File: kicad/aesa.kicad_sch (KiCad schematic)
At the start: 0 parts

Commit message: AD7606C-16, one sheet per repeated block, clock buffering, first simulations
- ADC: AD7606C-16 in software mode (OS pins high, WR held high, DB11/SDI on
  shared ADC_SDI), 33 R source resistors on DOUTA/DOUTB/BUSY.
- Every repeated block is its own reused sheet: tx_group x16, en_buf x4,
  clk_buf x7, mic x8 (replaces tx_shift, tx_drivers, mems). Sheets other than
  channel are generated by scripts/build_cells.py and scripts/build_power.py.
- Headers: GND conductors either side of every clock, ADC_SDI, idle pulls,
  DNP RC terminations as fallback.
- Power: 3V3_MIC ferrite filter moved to the power sheet with LED, test point
  and flag.
- Simulations (LTspice, sim/): RX chain gain/noise, TX burst and recovery,
  clock signal integrity; results in docs/simulation-1.md. FPGA ribbon outputs
  changed to DRIVE 4 after simulation.
- Brief, CLAUDE.md, review status and SKiDL reference spec updated.
  ERC: 0 violations, 1,701 parts.
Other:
- removed sheet MEMS mics
- removed sheet TX gate drivers
- removed sheet TX shift registers
- added sheet CLKB1 (clk_buf.kicad_sch)
- added sheet CLKB2 (clk_buf.kicad_sch)
- added sheet CLKB3 (clk_buf.kicad_sch)
- added sheet CLKB4 (clk_buf.kicad_sch)
- added sheet CLKB5 (clk_buf.kicad_sch)
- added sheet CLKB6 (clk_buf.kicad_sch)
- added sheet CLKB7 (clk_buf.kicad_sch)
- added sheet MIC1 (mic.kicad_sch)
- added sheet MIC2 (mic.kicad_sch)
- added sheet MIC3 (mic.kicad_sch)
- added sheet MIC4 (mic.kicad_sch)
- added sheet MIC5 (mic.kicad_sch)
- added sheet MIC6 (mic.kicad_sch)
- added sheet MIC7 (mic.kicad_sch)
- added sheet MIC8 (mic.kicad_sch)
- added sheet TXEN1 (en_buf.kicad_sch)
- added sheet TXEN2 (en_buf.kicad_sch)
- added sheet TXEN3 (en_buf.kicad_sch)
- added sheet TXEN4 (en_buf.kicad_sch)
- added sheet TXG01 (tx_group.kicad_sch)
- added sheet TXG02 (tx_group.kicad_sch)
- added sheet TXG03 (tx_group.kicad_sch)
- added sheet TXG04 (tx_group.kicad_sch)
- added sheet TXG05 (tx_group.kicad_sch)
- added sheet TXG06 (tx_group.kicad_sch)
- added sheet TXG07 (tx_group.kicad_sch)
- added sheet TXG08 (tx_group.kicad_sch)
- added sheet TXG09 (tx_group.kicad_sch)
- added sheet TXG10 (tx_group.kicad_sch)
- added sheet TXG11 (tx_group.kicad_sch)
- added sheet TXG12 (tx_group.kicad_sch)
- added sheet TXG13 (tx_group.kicad_sch)
- added sheet TXG14 (tx_group.kicad_sch)
- added sheet TXG15 (tx_group.kicad_sch)
- added sheet TXG16 (tx_group.kicad_sch)
- sheet ADC1 ports: added CONVST, SCLK; removed none
- sheet ADC2 ports: added CONVST, SCLK; removed none
- sheet ADC3 ports: added CONVST, SCLK; removed none
- sheet ADC4 ports: added CONVST, SCLK; removed none
- sheet ADC5 ports: added CONVST, SCLK; removed none
- sheet ADC6 ports: added CONVST, SCLK; removed none
- sheet ADC7 ports: added CONVST, SCLK; removed none
- sheet ADC8 ports: added CONVST, SCLK; removed none

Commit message: Block-diagram top page, power review fixes, readable sheets
Top level
- Page 1 is now a block diagram of the signal flow (FPGA -> headers ->
  clock buffers / TX drive -> transceivers -> ADCs -> FPGA, mics, power).
- New group sheets hold the reused cells: tx (16 tx_group + 4 en_buf),
  array (64 channel), adcs (8 adc), mics (8 mic), clocks (7 clk_buf).
  Power and headers stay directly under the top. All written by gen_top.py,
  which now also survives a kicad-cli re-save of a cell sheet.

Power (review findings)
- Polyfuse 1812L200/16DR (16 V), TPS65131RGER stated explicitly, input caps
  2 x 10u 1206, 50 V caps on 12 V, inductor values carry minimum Isat.
- +3V3: TLV75733P (ceramic-stable) replaces TLV1117-33.
- New JP5/JP6 isolate +-6V5; every rail: REG node -> jumper -> rail with TP,
  LED (not on analog LDOs) and PWR_FLAG.
- Power sheet is now generated by build_cells.py in a 2x3 block layout
  (build_power.py removed).

Readability and small fixes
- Rails on sideways pins use labelled flags; sideways GND symbols hide text.
- tx_group: 595 outputs wired straight to the drivers.
- Title blocks on every sheet; channel sheet notes and field placement fixed
  (sch_fields.py --only, sch_annotate.py).
- ADC_SDI 10k pull-down, ADC reset/DOUT notes, mic cap 50 V.
- ERC 0 violations, 1,704 parts. PDFs: docs/schematics/00..13.
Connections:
- no-connect marks 7 -> 0
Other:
- removed sheet ADC1
- removed sheet ADC2
- removed sheet ADC3
- removed sheet ADC4
- removed sheet ADC5
- removed sheet ADC6
- removed sheet ADC7
- removed sheet ADC8
- removed sheet AXU3EGB headers
- removed sheet CH01
- removed sheet CH02
- removed sheet CH03
- removed sheet CH04
- removed sheet CH05
- removed sheet CH06
- removed sheet CH07
- removed sheet CH08
- removed sheet CH09
- removed sheet CH10
- removed sheet CH11
- removed sheet CH12
- removed sheet CH13
- removed sheet CH14
- removed sheet CH15
- removed sheet CH16
- removed sheet CH17
- removed sheet CH18
- removed sheet CH19
- removed sheet CH20
- removed sheet CH21
- removed sheet CH22
- removed sheet CH23
- removed sheet CH24
- removed sheet CH25
- removed sheet CH26
- removed sheet CH27
- removed sheet CH28
- removed sheet CH29
- removed sheet CH30
- removed sheet CH31
- removed sheet CH32
- removed sheet CH33
- removed sheet CH34
- removed sheet CH35
- removed sheet CH36
- removed sheet CH37
- removed sheet CH38
- removed sheet CH39
- removed sheet CH40
- removed sheet CH41
- removed sheet CH42
- removed sheet CH43
- removed sheet CH44
- removed sheet CH45
- removed sheet CH46
- removed sheet CH47
- removed sheet CH48
- removed sheet CH49
- removed sheet CH50
- removed sheet CH51
- removed sheet CH52
- removed sheet CH53
- removed sheet CH54
- removed sheet CH55
- removed sheet CH56
- removed sheet CH57
- removed sheet CH58
- removed sheet CH59
- removed sheet CH60
- removed sheet CH61
- removed sheet CH62
- removed sheet CH63
- removed sheet CH64
- removed sheet CLKB1
- removed sheet CLKB2
- removed sheet CLKB3
- removed sheet CLKB4
- removed sheet CLKB5
- removed sheet CLKB6
- removed sheet CLKB7
- removed sheet MIC1
- removed sheet MIC2
- removed sheet MIC3
- removed sheet MIC4
- removed sheet MIC5
- removed sheet MIC6
- removed sheet MIC7
- removed sheet MIC8
- removed sheet TXEN1
- removed sheet TXEN2
- removed sheet TXEN3
- removed sheet TXEN4
- removed sheet TXG01
- removed sheet TXG02
- removed sheet TXG03
- removed sheet TXG04
- removed sheet TXG05
- removed sheet TXG06
- removed sheet TXG07
- removed sheet TXG08
- removed sheet TXG09
- removed sheet TXG10
- removed sheet TXG11
- removed sheet TXG12
- removed sheet TXG13
- removed sheet TXG14
- removed sheet TXG15
- removed sheet TXG16
- added sheet ADCs (adcs.kicad_sch)
- added sheet Clock buffers (clocks.kicad_sch)
- added sheet FPGA headers J1/J2 (headers.kicad_sch)
- added sheet MEMS mics (mics.kicad_sch)
- added sheet TX drive (tx.kicad_sch)
- added sheet Transceivers (array.kicad_sch)
- note added: "(ADCs)"
- note added: "(TX, mics)"
- note added: "(off-board)"
- note added: "0 / 15 V"
- note added: "1. The FPGA streams one TX bit per element (16 serial lines, 10 MHz) and the clocks."
- note added: "12 V jack -> +5V, +-6V5, +-5VA (analog), VDRV 15 V (TX), +3V3, 3V3_MIC."
- note added: "16 x 74HCT595 + 32 x UCC27524"
- note added: "2 ribbons"
- note added: "2. TX drive: shift registers latch the bits; gate drivers switch each element between 0 and 15 V."
- note added: "3. Transceivers: the 64 CUSA-TR65 elements emit 40 kHz; echoes return to the same elements."
- note added: "4 x enable buffer"
- note added: "4. The diode T/R switch and limiter protect the receiver; amplifier + 40 kHz band-pass give x22."
- note added: "40 kHz"
- note added: "5. ADCs: 8 x AD7606C-16 sample all 64 channels at 200 kSPS (raw waveform, amplitude and phase)."
- note added: "6. The samples go back to the FPGA over the ribbon, which forms the beams. 8 MEMS mics add wideband audio."
- note added: "64 x: T/R diodes, CUSA-TR65,"
- note added: "7 x 74LVC2G34, 33 R"
- note added: "8 x AD7606C-16, 200 kSPS"
- note added: "8 x SPH0641 PDM"
- note added: "ADC readout"
- note added: "ADC_DOUTA/B 1-8, BUSY"
- note added: "ALINX AXU3EGB"
- note added: "Air /"
- note added: "Click a block to open it. Repeated parts are one sheet each: channel x64, adc x8, tx_group x16, en_buf x4, clk_buf x7, mic x8."
- note added: "DRV1-64"
- note added: "Every rail: test point, isolation jumper, LED (not on the analog LDOs)."
- note added: "Hybrid 8x8 ultrasonic AESA: how the signal flows"
- note added: "J1 = AXU3EGB J15"
- note added: "J2 = AXU3EGB J16"
- note added: "MIC_DATA0-3 (PDM)"
- note added: "PDM clock"
- note added: "RX1-64"
- note added: "SCK, LATCH"
- note added: "SCLK, CONVST"
- note added: "TX timing,"
- note added: "TX_SDI0-15, TX_EN, /OE, /CLR"
- note added: "Zynq UltraScale+"
- note added: "beamforming,"
- note added: "clocks"
- note added: "echo"
- note added: "echo x22"
- note added: "limiter, x6 amp, 40 kHz band-pass"
- note added: "target"
- note removed: "Hybrid 8x8 ultrasonic AESA: 64 transceiver channels (CH01..CH64, one sheet reused 64 times), 8 MEMS mics, 8 ADCs. Source of truth: this KiCad hierarchy; skidl/channel.py is the reference spec."
- company: (none) -> Hybrid 8x8 ultrasonic AESA
- title: Ultrasonic AESA front end -> Hybrid 8x8 ultrasonic AESA: block diagram

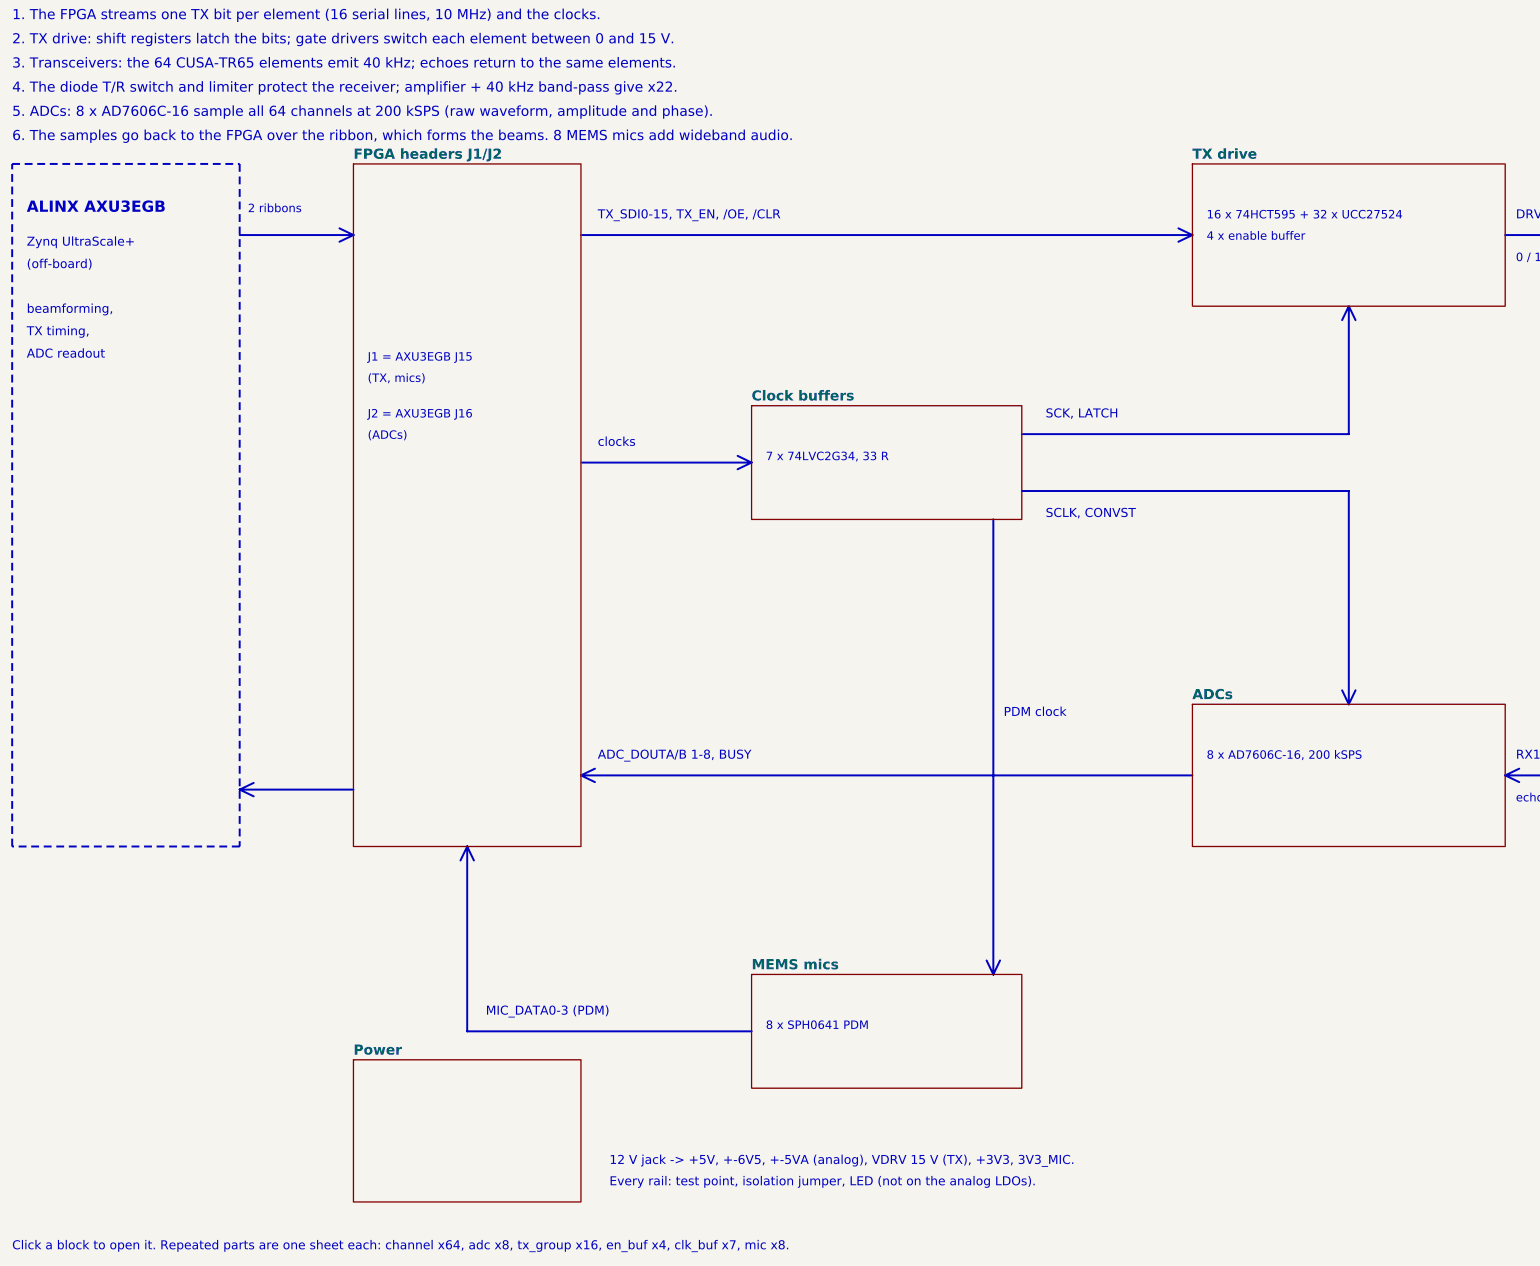
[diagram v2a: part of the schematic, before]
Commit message: Switch to 16 x TLV320ADC5140, +3V3A rail, 3 A buck, datasheet library, transducer DNP
- ADC: 8 x AD7606C-16 ($470/board) -> 16 x TI TLV320ADC5140 at 192 kSPS ($50/board): TDM slave on a
  shared BCLK/FSYNC, I2C (SCL + 4 SDA groups), 2k/1k + 100 nF input network; project symbol from
  scripts/make_symbols.py; 9 clock buffers; J2 remapped
- power: +3V3A (second TPS7A4700, ANY-OUT 3.3 V); +5V buck TPS54202 -> TPS54302 (3 A), L1 10 uH 5 A
- checks and simulations updated for the new ADC input (all 18 checks and 10 sims pass)
- docs/datasheets: a PDF for every part, kept in step by scripts/datasheets.py (run by bom.py)
- design brief section 5a: interface bandwidth budget (no bus is a bottleneck; TX_EDGE = 1)
- CUSA-TR65 marked DNP for JLCPCB (hand-soldered), priced at DigiKey 100+
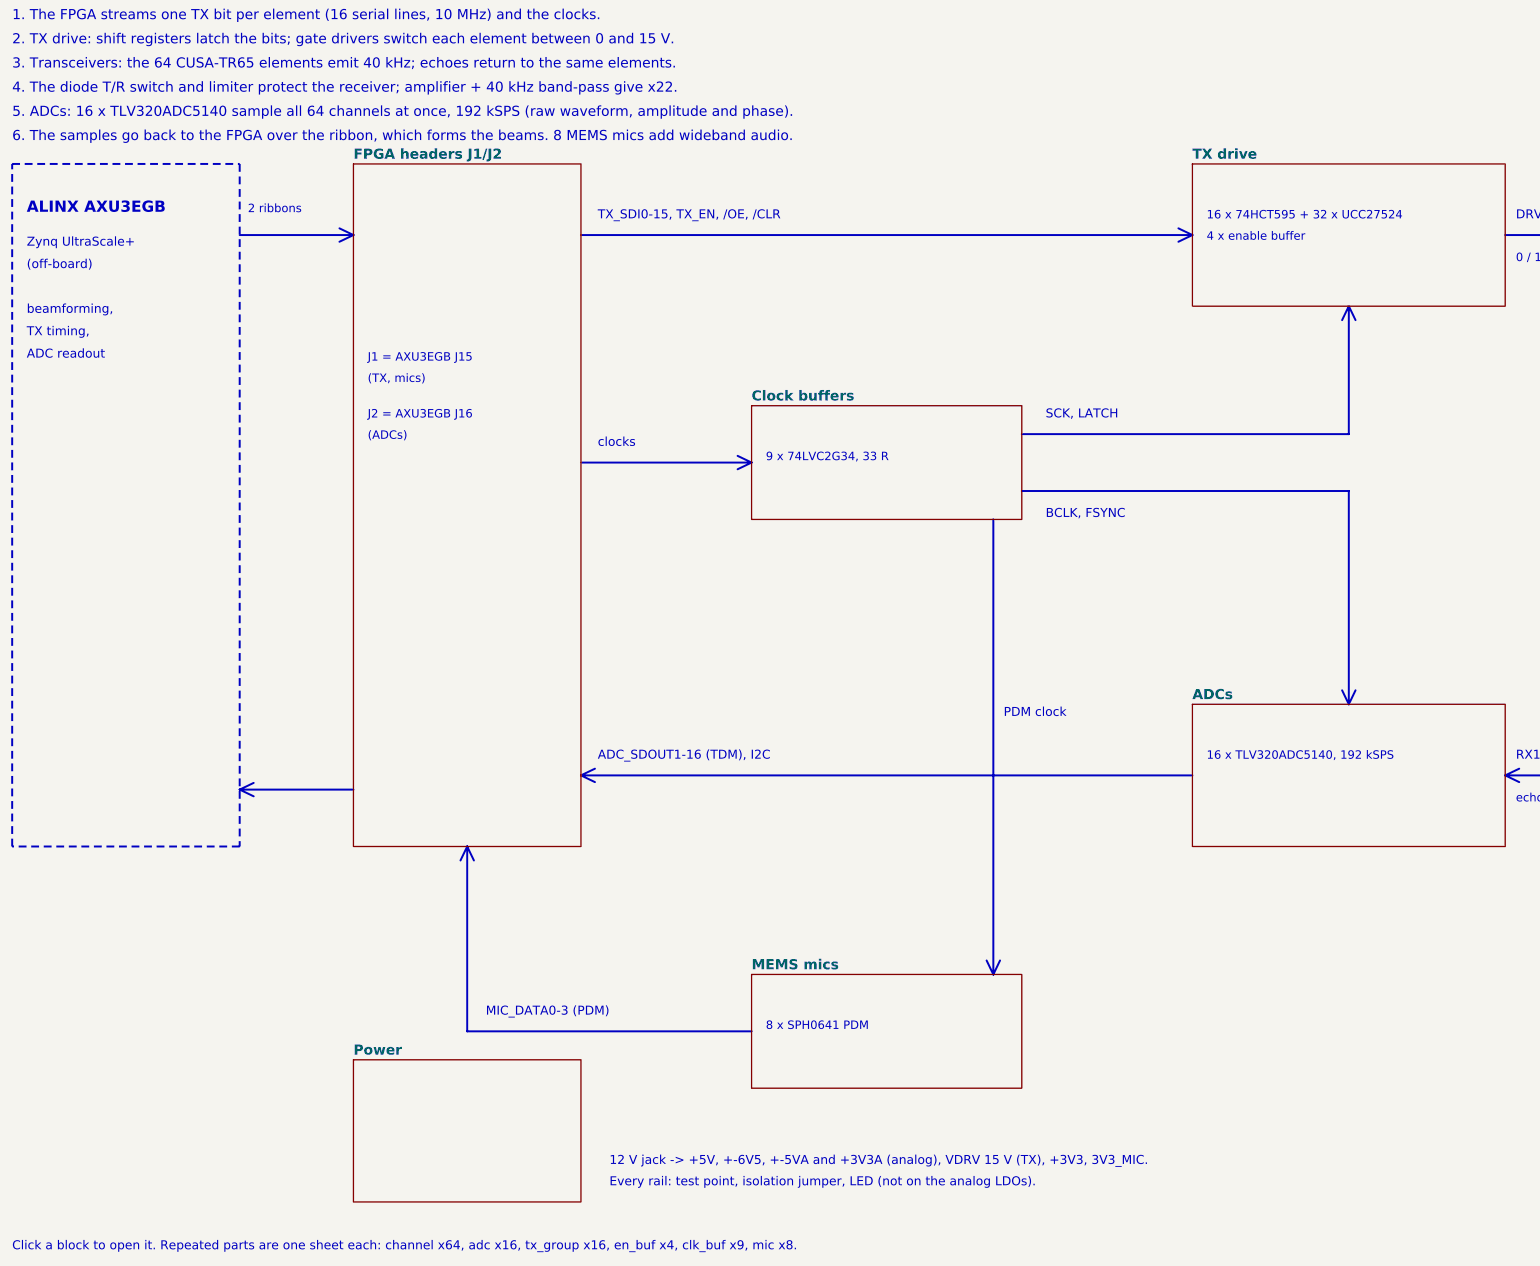
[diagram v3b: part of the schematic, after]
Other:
- note added: "12 V jack -> +5V, +-6V5, +-5VA and +3V3A (analog), VDRV 15 V (TX), +3V3, 3V3_MIC."
- note added: "16 x TLV320ADC5140, 192 kSPS"
- note added: "5. ADCs: 16 x TLV320ADC5140 sample all 64 channels at once, 192 kSPS (raw waveform, amplitude and phase)."
- note added: "9 x 74LVC2G34, 33 R"
- note added: "ADC_SDOUT1-16 (TDM), I2C"
- note added: "BCLK, FSYNC"
- note added: "Click a block to open it. Repeated parts are one sheet each: channel x64, adc x16, tx_group x16, en_buf x4, clk_buf x9, mic x8."
- note removed: "12 V jack -> +5V, +-6V5, +-5VA (analog), VDRV 15 V (TX), +3V3, 3V3_MIC."
- note removed: "5. ADCs: 8 x AD7606C-16 sample all 64 channels at 200 kSPS (raw waveform, amplitude and phase)."
- note removed: "7 x 74LVC2G34, 33 R"
- note removed: "8 x AD7606C-16, 200 kSPS"
- note removed: "ADC_DOUTA/B 1-8, BUSY"
- note removed: "Click a block to open it. Repeated parts are one sheet each: channel x64, adc x8, tx_group x16, en_buf x4, clk_buf x7, mic x8."
- note removed: "SCLK, CONVST"
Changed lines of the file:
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@@
 		)
 	)
-	(text "5. ADCs: 8 x AD7606C-16 sample all 64 channels at 200 kSPS (raw waveform, amplitude and phase)."
+	(text "5. ADCs: 16 x TLV320ADC5140 sample all 64 channels at once, 192 kSPS (raw waveform, amplitude and phase)."
 		(exclude_from_sim no)
 		(at 25.40 52.84 0)
@@
 		)
 	)
-	(text "SCLK, CONVST"
+	(text "BCLK, FSYNC"
 		(exclude_from_sim no)
 		(at 210.00 124.46 0)
@@
 		)
 	)
-	(text "ADC_DOUTA/B 1-8, BUSY"
+	(text "ADC_SDOUT1-16 (TDM), I2C"
 		(exclude_from_sim no)
 		(at 130.00 167.64 0)
@@
 		)
 	)
-	(text "8 x AD7606C-16, 200 kSPS"
+	(text "16 x TLV320ADC5140, 192 kSPS"
 		(exclude_from_sim no)
 		(at 238.76 167.64 0)
@@
 		)
 	)
-	(text "7 x 74LVC2G34, 33 R"
+	(text "9 x 74LVC2G34, 33 R"
 		(exclude_from_sim no)
 		(at 160.02 114.30 0)
@@
 		)
 	)
-	(text "12 V jack -> +5V, +-6V5, +-5VA (analog), VDRV 15 V (TX), +3V3, 3V3_MIC."
+	(text "12 V jack -> +5V, +-6V5, +-5VA and +3V3A (analog), VDRV 15 V (TX), +3V3, 3V3_MIC."
 		(exclude_from_sim no)
 		(at 132.08 240.03 0)
@@
 		)
 	)
-	(text "Click a block to open it. Repeated parts are one sheet each: channel x64, adc x8, tx_group x16, en_buf x4, clk_buf x7, mic x8."
+	(text "Click a block to open it. Repeated parts are one sheet each: channel x64, adc x16, tx_group x16, en_buf x4, clk_buf x9, mic x8."
 		(exclude_from_sim no)
 		(at 25.40 255.27 0)
@@
 			(project "aesa"
 				(path "/35d88121-1d5f-4a62-9009-788ea6bf93dd"
-					(page "11")
+					(page "13")
 				)
 			)
@@
 			(project "aesa"
 				(path "/35d88121-1d5f-4a62-9009-788ea6bf93dd"
-					(page "32")
+					(page "34")
 				)
 			)
@@
 			(project "aesa"
 				(path "/35d88121-1d5f-4a62-9009-788ea6bf93dd"
-					(page "97")
+					(page "99")
 				)
 			)
@@
 			(project "aesa"
 				(path "/35d88121-1d5f-4a62-9009-788ea6bf93dd"
-					(page "106")
+					(page "116")
 				)
 			)
@@
 			(project "aesa"
 				(path "/35d88121-1d5f-4a62-9009-788ea6bf93dd"
-					(page "115")
-				)
-			)
+					(page "125")
+				)
+			)
